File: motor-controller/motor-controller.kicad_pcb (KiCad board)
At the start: 2 copper layers, 65.4 x 35.6 mm, 34 parts, among them J1 Molex 172043-0201 R/A, J2 Molex 172043-0302 R/A, J3 MCU-IO, Q1 2N3904, U1 DRV10983PWP, U2 TLP291-4, U3 SI8600AC

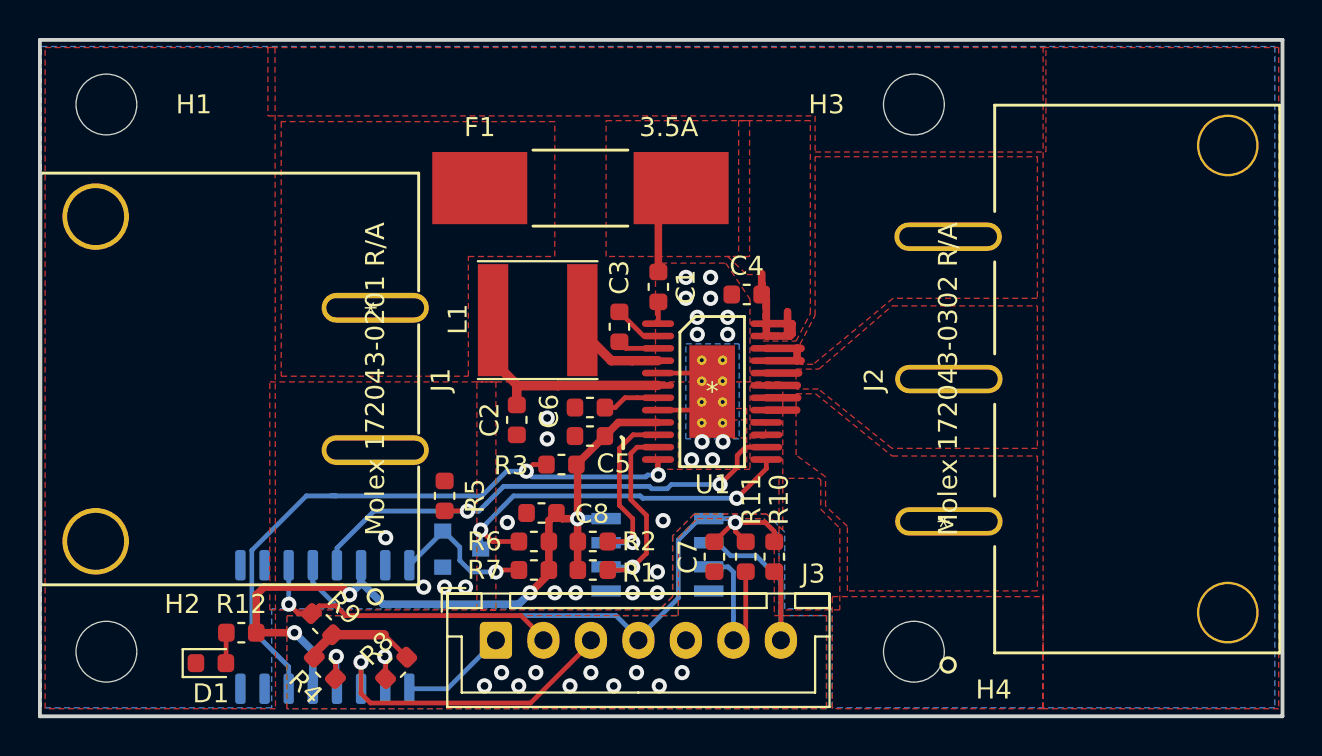
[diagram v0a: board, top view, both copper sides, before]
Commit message: Preparation for fabrication.  Changed PCB silkscreen and added part numbers to schematic.
Added board description, version number, and date to PCB silkscreen.
Added Digi-Key part numbers and mating connectors as symbol attributes
for some connectors in schematic.
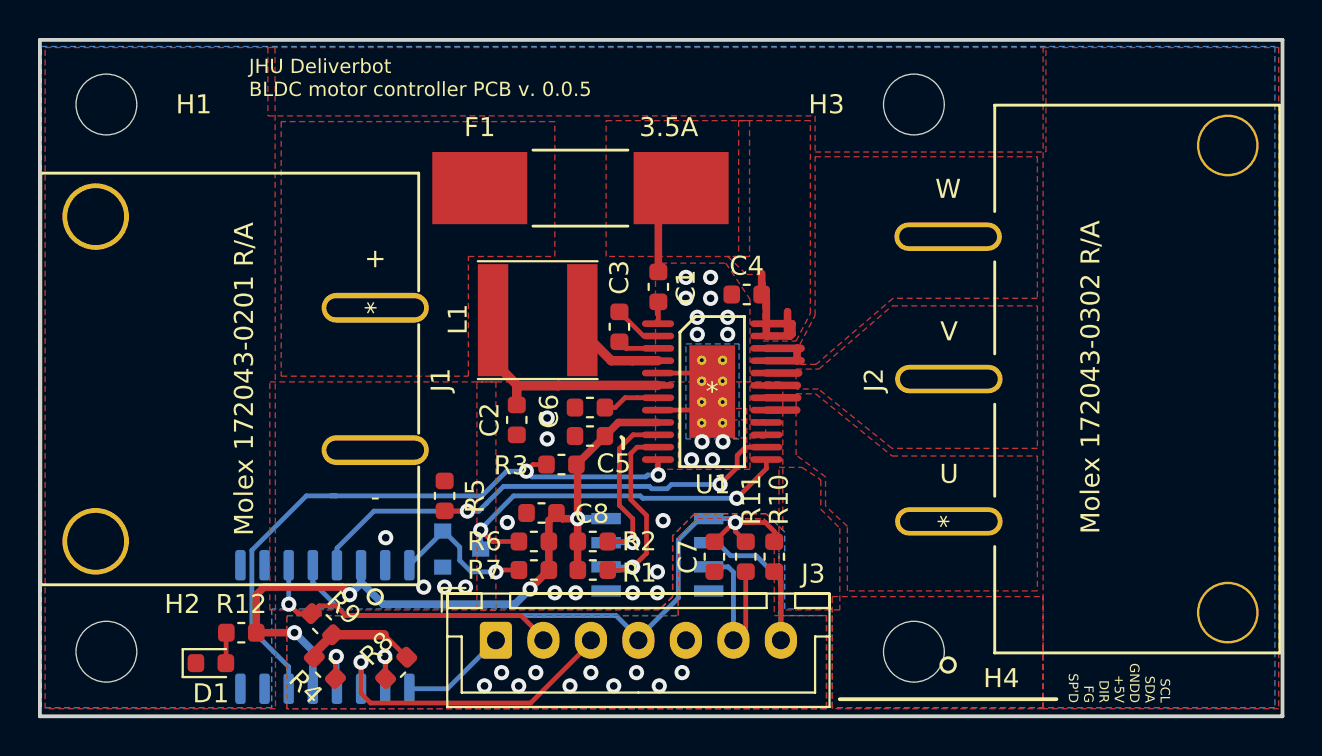
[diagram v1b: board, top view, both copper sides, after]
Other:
- board text added: "+"
- board text added: "-"
- board text added: "12 April 2021"
- board text added: "JHU Deliverbot BLDC motor controller PCB v. 0.0.5"
- board text added: "SCL SDA GNDD +5V DIR FG SP'D"
- board text added: "U"
- board text added: "V"
- board text added: "W"
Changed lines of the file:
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@@
   (general
     (thickness 1.6)
-    (drawings 19)
-    (tracks 279)
+    (drawings 28)
+    (tracks 280)
     (zones 0)
     (modules 34)
@@
   (title_block
     (title "Brushless DC Motor Controller")
-    (date 2021-01-13)
-    (rev 0.0.2)
+    (date 2021-04-12)
+    (rev 0.0.5)
     (company "JHU Deliverbot Project")
     (comment 1 "Drafted by @avnoks")
@@
     (tags "mounting hole 3.2mm no annular m3")
     (attr virtual)
-    (fp_text reference H4 (at 4.2 2) (layer F.SilkS)
+    (fp_text reference H4 (at 4.6 1.4 180) (layer F.SilkS)
       (effects (font (size 1 1) (thickness 0.15)))
     )
@@
       (effects (font (size 1 1) (thickness 0.15)))
     )
-    (fp_text value "Molex 172043-0201 R/A" (at -3.745 0 90) (layer F.SilkS)
+    (fp_text value "Molex 172043-0201 R/A" (at -3.745 -6.9 90) (layer F.SilkS)
       (effects (font (size 1 1) (thickness 0.15)))
     )
@@
       (effects (font (size 1 1) (thickness 0.15)))
     )
-    (fp_text value "Molex 172043-0302 R/A" (at 7.493 0 90) (layer F.SilkS)
+    (fp_text value "Molex 172043-0302 R/A" (at 7.593 7.4981 90) (layer F.SilkS)
       (effects (font (size 1 1) (thickness 0.15)))
     )
@@
       (rotate (xyz 0 0 0))
     )
+  )
+  (gr_text "12 April 2021" (at 173.1 118.8) (layer B.SilkS)
+    (effects (font (size 0.75 0.75) (thickness 0.15)) (justify mirror))
+  )
+  (gr_text "JHU Deliverbot\nBLDC motor controller PCB v. 0.0.5 " (at 128 87) (layer F.SilkS)
+    (effects (font (size 0.75 0.75) (thickness 0.15)) (justify left))
+  )
+  (gr_line (start 170.5 119.7) (end 159.1 119.7) (layer F.SilkS) (width 0.2))
+  (gr_text "SCL\nSDA\nGNDD\n+5V\nDIR\nFG\nSP'D\n" (at 173.8 119.9 270) (layer F.SilkS)
+    (effects (font (size 0.5 0.5) (thickness 0.125)) (justify right))
+  )
+  (gr_text - (at 134.65 109.05) (layer F.SilkS)
+    (effects (font (size 1 1) (thickness 0.15)))
+  )
+  (gr_text + (at 134.65 96.5) (layer F.SilkS)
+    (effects (font (size 1 1) (thickness 0.15)))
+  )
+  (gr_text U (at 164.85 107.85) (layer F.SilkS)
+    (effects (font (size 1 1) (thickness 0.15)))
+  )
+  (gr_text V (at 164.85 100.35) (layer F.SilkS)
+    (effects (font (size 1 1) (thickness 0.15)))
+  )
+  (gr_text W (at 164.8 92.85) (layer F.SilkS)
+    (effects (font (size 1 1) (thickness 0.15)))
   )
   (gr_line (start 147.7 106) (end 147.6 105.9) (layer F.SilkS) (width 0.2))
@@
   (segment (start 145.55 100.358272) (end 147.07673 101.885002) (width 0.5) (layer F.Cu) (net 11))
   (segment (start 145.55 99.75) (end 145.55 100.358272) (width 0.5) (layer F.Cu) (net 11))
-  (via (at 142.8 114.1) (size 0.8) (drill 0.4) (layers F.Cu B.Cu) (net 12))
+  (via (at 142.8 113.9) (size 0.8) (drill 0.4) (layers F.Cu B.Cu) (net 12))
   (via (at 145.3 110.2) (size 0.8) (drill 0.4) (layers F.Cu B.Cu) (net 12))
   (segment (start 146.795 110.2) (end 146.8 110.195) (width 0.25) (layer B.Cu) (net 12))
@@
   (segment (start 143.7875 111.4) (end 143.7875 110.3) (width 0.4) (layer F.Cu) (net 12))
   (segment (start 143.7875 111.4) (end 143.7875 112.9) (width 0.4) (layer F.Cu) (net 12))
-  (segment (start 143.7875 113.1125) (end 142.8 114.1) (width 0.4) (layer F.Cu) (net 12))
   (segment (start 143.7875 112.9) (end 143.7875 113.1125) (width 0.4) (layer F.Cu) (net 12))
   (segment (start 133.905 113.55) (end 133.905 112.65) (width 0.4) (layer B.Cu) (net 12))
   (segment (start 135.055 114.7) (end 135.055 114.7) (width 0.4) (layer B.Cu) (net 12))
-  (segment (start 142.2 114.7) (end 135.055 114.7) (width 0.4) (layer B.Cu) (net 12))
-  (segment (start 142.8 114.1) (end 142.2 114.7) (width 0.4) (layer B.Cu) (net 12))
   (segment (start 135.055 114.7) (end 133.905 113.55) (width 0.4) (layer B.Cu) (net 12))
   (via (at 133.3 114.2) (size 0.8) (drill 0.4) (layers F.Cu B.Cu) (net 12))
@@
   (segment (start 131.365 117.165) (end 130.4 116.2) (width 0.4) (layer B.Cu) (net 12))
   (segment (start 131.365 119.15) (end 131.365 117.165) (width 0.4) (layer B.Cu) (net 12))
+  (segment (start 142.8 113.8875) (end 143.7875 112.9) (width 0.4) (layer F.Cu) (net 12))
+  (segment (start 142.8 113.9) (end 142.8 113.8875) (width 0.4) (layer F.Cu) (net 12))
+  (segment (start 142.8 113.9) (end 142 114.7) (width 0.4) (layer B.Cu) (net 12))
+  (segment (start 142 114.7) (end 135.055 114.7) (width 0.4) (layer B.Cu) (net 12))
   (segment (start 148.5 116.475) (end 148.5 116.6) (width 0.25) (layer B.Cu) (net 14))
   (via (at 153.6 110.4) (size 0.8) (drill 0.4) (layers F.Cu B.Cu) (net 14))
@@
       (pts
         (xy 157 102.075) (xy 157 101.025) (xy 157.8 99.5) (xy 157.8 91.15) (xy 169.5 91.15)
-        (xy 169.5 98.6) (xy 161.9 98.6) (xy 157.7 102.075)
+        (xy 169.5 98.6) (xy 161.9 98.6) (xy 157.85 102.075)
       )
     )
@@
     (polygon
       (pts
-        (xy 155.9 108.075) (xy 158 108.075) (xy 158.1 108.175) (xy 158.1 109.7) (xy 159.1 110.7)
-        (xy 159.1 115) (xy 155.9 115)
+        (xy 155.9 107.5) (xy 157.1 107.5) (xy 158 108.075) (xy 158.1 108.175) (xy 158.1 109.7)
+        (xy 159.1 110.7) (xy 159.1 115) (xy 155.9 115)
       )
     )

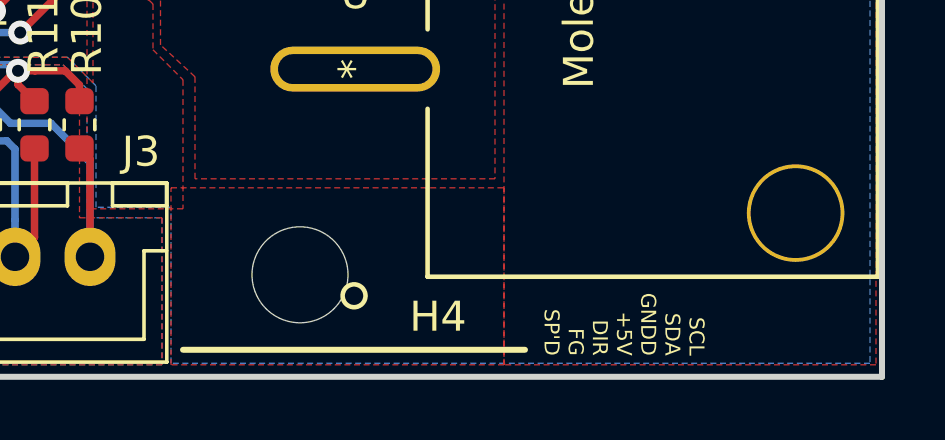
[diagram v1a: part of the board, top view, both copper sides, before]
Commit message: Adjusted silkscreen text size.
Enlargened size of all silkscreen text smaller than 0.8mmx0.8mm 0.15mm
thickness to those dimensions, which are the minimum legible silkscreen
resolution offered by JLCPCB's process.
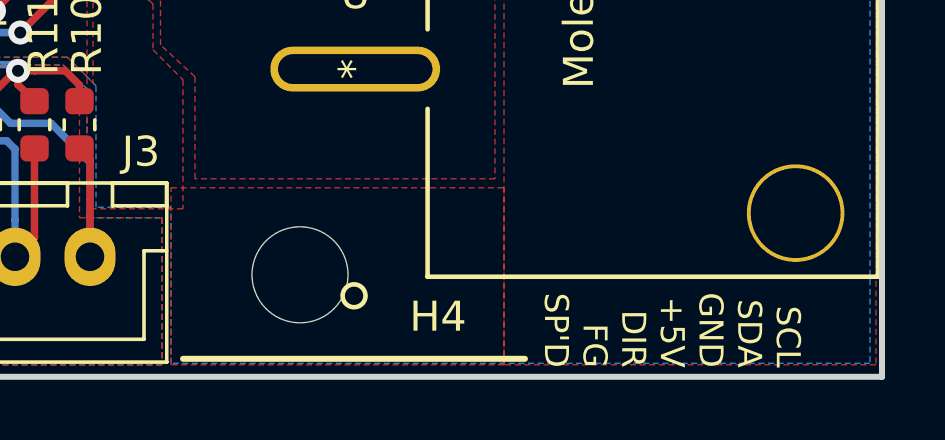
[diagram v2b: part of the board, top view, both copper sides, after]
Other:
- board text added: "JLCJLCJLCJLC"
- board text added: "SCL SDA GND +5V DIR FG SP'D"
- board text removed: "SCL SDA GNDD +5V DIR FG SP'D"
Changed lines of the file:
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@@
   (general
     (thickness 1.6)
-    (drawings 28)
+    (drawings 29)
     (tracks 280)
     (zones 0)
@@
     (38 B.Mask user)
     (39 F.Mask user)
-    (40 Dwgs.User user hide)
+    (40 Dwgs.User user)
     (41 Cmts.User user)
     (42 Eco1.User user)
@@
     (pcbplotparams
       (layerselection 0x010fc_ffffffff)
-      (usegerberextensions false)
+      (usegerberextensions true)
       (usegerberattributes false)
       (usegerberadvancedattributes false)
@@
       (psa4output false)
       (plotreference true)
-      (plotvalue true)
+      (plotvalue false)
       (plotinvisibletext false)
       (padsonsilk false)
-      (subtractmaskfromsilk false)
+      (subtractmaskfromsilk true)
       (outputformat 1)
       (mirror false)
-      (drillshape 1)
+      (drillshape 0)
       (scaleselection 1)
-      (outputdirectory ""))
+      (outputdirectory "gerber/"))
   )
   (net 0 "")
@@
     )
   )
+  (gr_text JLCJLCJLCJLC (at 119.1 103 270) (layer B.SilkS)
+    (effects (font (size 0.8 0.8) (thickness 0.15)) (justify mirror))
+  )
   (gr_text "12 April 2021" (at 173.1 118.8) (layer B.SilkS)
-    (effects (font (size 0.75 0.75) (thickness 0.15)) (justify mirror))
+    (effects (font (size 0.8 0.8) (thickness 0.15)) (justify mirror))
   )
   (gr_text "JHU Deliverbot\nBLDC motor controller PCB v. 0.0.5 " (at 128 87) (layer F.SilkS)
     (effects (font (size 0.75 0.75) (thickness 0.15)) (justify left))
   )
-  (gr_line (start 170.5 119.7) (end 159.1 119.7) (layer F.SilkS) (width 0.2))
-  (gr_text "SCL\nSDA\nGNDD\n+5V\nDIR\nFG\nSP'D\n" (at 173.8 119.9 270) (layer F.SilkS)
-    (effects (font (size 0.5 0.5) (thickness 0.125)) (justify right))
+  (gr_line (start 170.5 120) (end 159.1 120) (layer F.SilkS) (width 0.2))
+  (gr_text "SCL\nSDA\nGND\n+5V\nDIR\nFG\nSP'D\n" (at 175.4 120.3 270) (layer F.SilkS)
+    (effects (font (size 0.8 0.8) (thickness 0.15)) (justify right))
   )
   (gr_text - (at 134.65 109.05) (layer F.SilkS)
